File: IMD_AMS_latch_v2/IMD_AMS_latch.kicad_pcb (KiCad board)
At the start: 2 copper layers, 66.9 x 59.9 mm, 39 parts, among them J1 Conn_01x04, J2 Conn_01x04, J3 Conn_01x04, J4 Conn_01x04, K1 SANYOU_SRD_Form_C, K2 SANYOU_SRD_Form_C, Q1 AO3400A, Q2 AO3400A, U1 MC14044BDR2G, U2 LM393

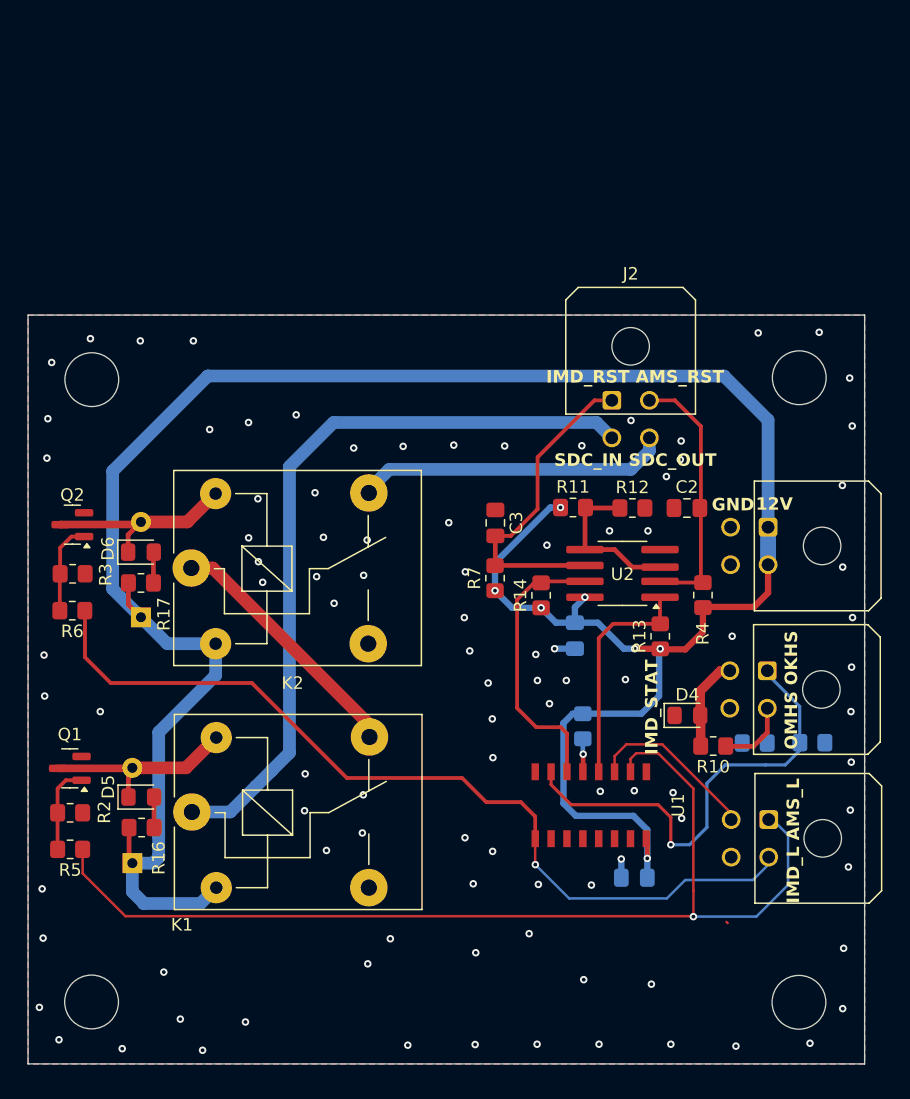
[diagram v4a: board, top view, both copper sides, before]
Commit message: fixed connectors
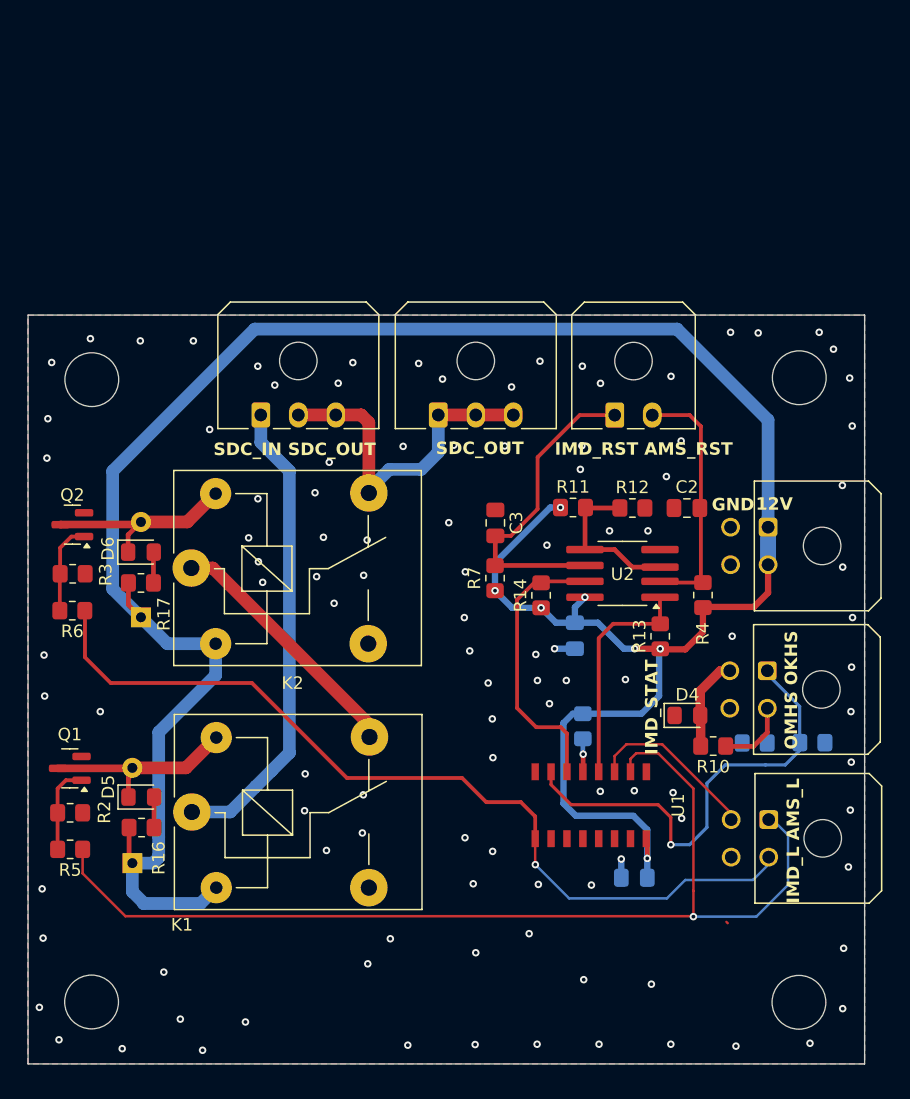
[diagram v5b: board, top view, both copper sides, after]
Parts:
- added J6: Conn_01x03, Connector_Molex:Molex_Micro-Fit_3.0_43650-0300_1x03_P3.00mm_Horizontal, F.Cu at (148.5, 63.7)
- added J7: Conn_01x02, Connector_Molex:Molex_Micro-Fit_3.0_43650-0200_1x02_P3.00mm_Horizontal, F.Cu at (176.8, 63.7)
- J2: value Conn_01x04 -> Conn_01x03; footprint Connector_Molex:Molex_Micro-Fit_3.0_43045-0400_2x02_P3.00mm_Horizontal -> Connector_Molex:Molex_Micro-Fit_3.0_43650-0300_1x03_P3.00mm_Horizontal
- moved J2 13.9 mm to (162.7, 63.7)
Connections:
- J2 pad 1: /IMD_reset_btn -> /SDC_OUT
- J2 pad 2: /AMS_reset_btn -> /SDC_OUT
- J2 pad 3: /SDC_IN -> /SDC_OUT
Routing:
- net /SDC_IN: track 60.4 -> 37.7 mm
- net +12V: track 198.0 -> 201.1 mm
- net /SDC_OUT: track 24.8 -> 27.3 mm
- net /AMS_reset_btn: track 21.0 -> 20.3 mm
- net GND: vias 99 -> 109
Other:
- board text added: "SDC_OUT"

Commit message: fixed connectors
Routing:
- net GND: vias 109 -> 110
- net (no net): vias 0 -> 1
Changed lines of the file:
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@@
 		)
+	)
+	(via
+		(at 172.94 32.83)
+		(size 0.6)
+		(drill 0.3)
+		(layers "F.Cu" "B.Cu")
+		(net 0)
 	)
 	(segment
@@
 		(size 0.6)
 		(drill 0.3)
+		(layers "F.Cu" "B.Cu")
+		(free yes)
+		(net 1)
+	)
+	(via
+		(at 177.29 77.77)
+		(size 0.6)
+		(drill 0.3)

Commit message: IMD AMS latch
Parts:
- moved Q2 43.6 mm to (159.4, 107.4), turned to -90 degrees
- moved R6 43.2 mm to (166.3, 107.4), turned to -90 degrees
- moved R3 43.1 mm to (163.4, 107.4), turned to 90 degrees
- moved D2 35.6 mm to (166.8, 101.9), turned to 180 degrees
- moved D6 35.5 mm to (161.6, 101.9), turned to 90 degrees
- moved R17 35.3 mm to (164.1, 101.9), turned to -90 degrees
- moved K1 23.4 mm to (139.7, 72.3), turned to -90 degrees
- moved K2 19.1 mm to (156.6, 89.2), turned to 90 degrees
- moved R5 18.5 mm to (149.3, 107.6), turned to -90 degrees
- moved Q1 18.4 mm to (142.9, 107.6), turned to -90 degrees
- moved R2 17.9 mm to (146.4, 107.6), turned to 90 degrees
- moved D1 12.6 mm to (150.4, 102.6), turned to 180 degrees
- moved R16 10.1 mm to (147.6, 101.9), turned to -90 degrees
- moved D5 9.86 mm to (145.2, 101.9), turned to 90 degrees
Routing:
- net /IMD_latch: track 69.8 -> 32.0 mm
- net /SDC_IN: track 37.7 -> 0.00 mm
- net /SDC_OUT: track 27.3 -> 0.00 mm
- net Net-(D1-A): track 16.1 -> 43.2 mm
- net +12V: track 201.1 -> 177.3 mm
- net Net-(K1-Pad4): track 20.4 -> 0.00 mm
- net /AMS_latch: track 85.6 -> 72.2 mm
- net Net-(D2-A): track 16.3 -> 27.5 mm
- net GND: track 3.27 -> 3.46 mm, vias 110 -> 81
- added copper zone on B.Cu, net /SDC_IN
- added copper zone on F.Cu, net /SDC_IN
- added copper zone on B.Cu, net /SDC_OUT
- added copper zone on F.Cu, net /SDC_OUT
- added copper zone on B.Cu, net Net-(K1-Pad4)
- added copper zone on F.Cu, net Net-(K1-Pad4)
